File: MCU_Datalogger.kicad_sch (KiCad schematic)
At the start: 25 parts, among them U1 24LC1025, U2 24LC1025, U3 DS1337S_, U4 ATMEGA328P-AU, Y1 Crystal, Y2 Crystal

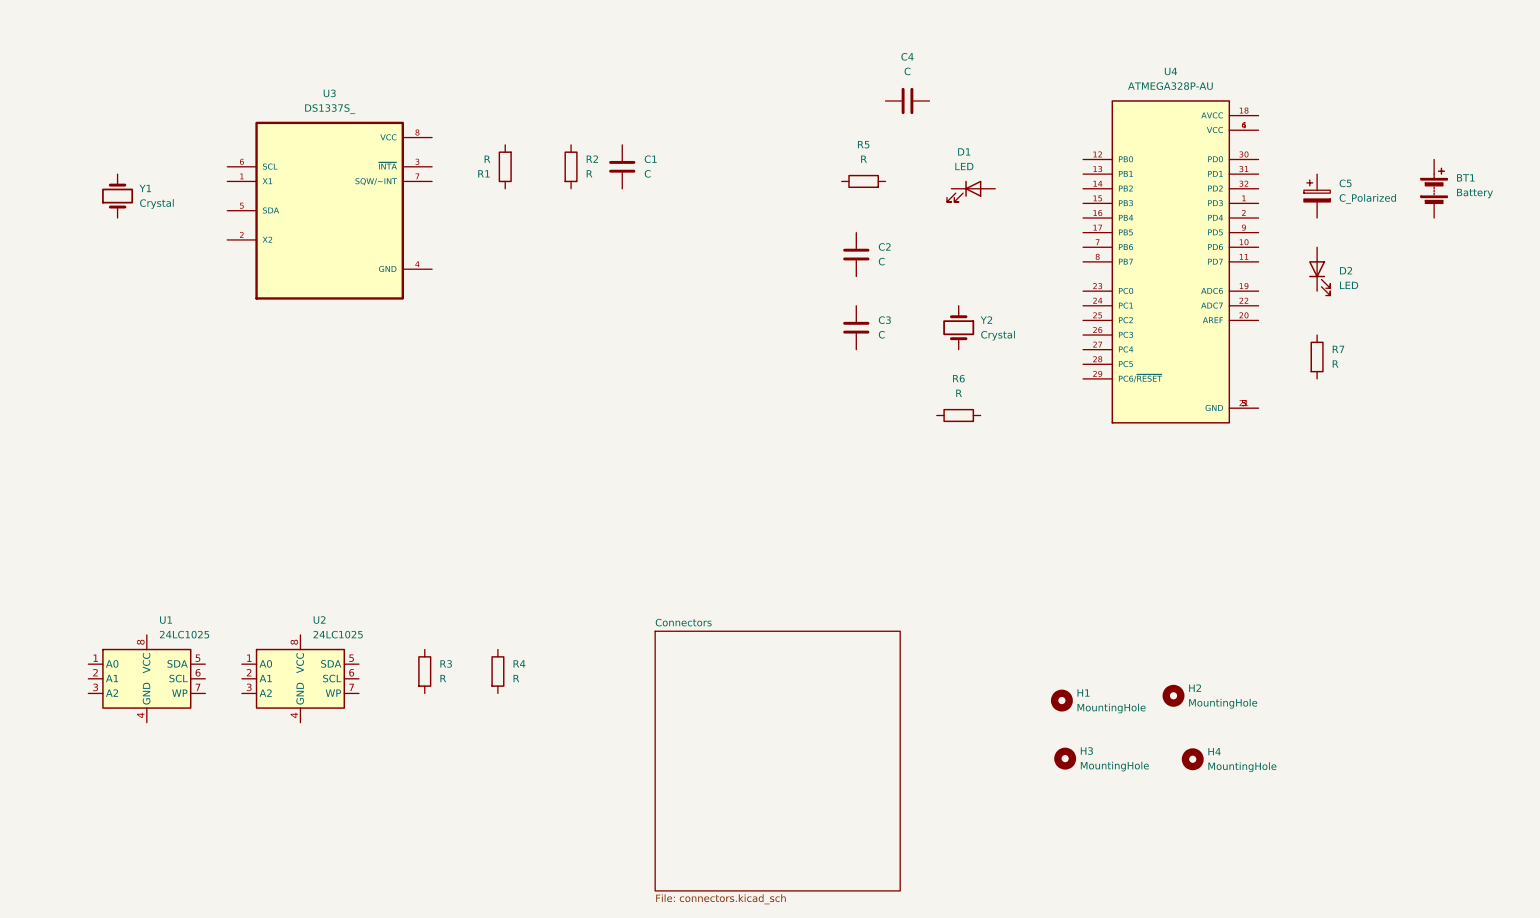
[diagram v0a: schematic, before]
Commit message: Assigned footprints to components
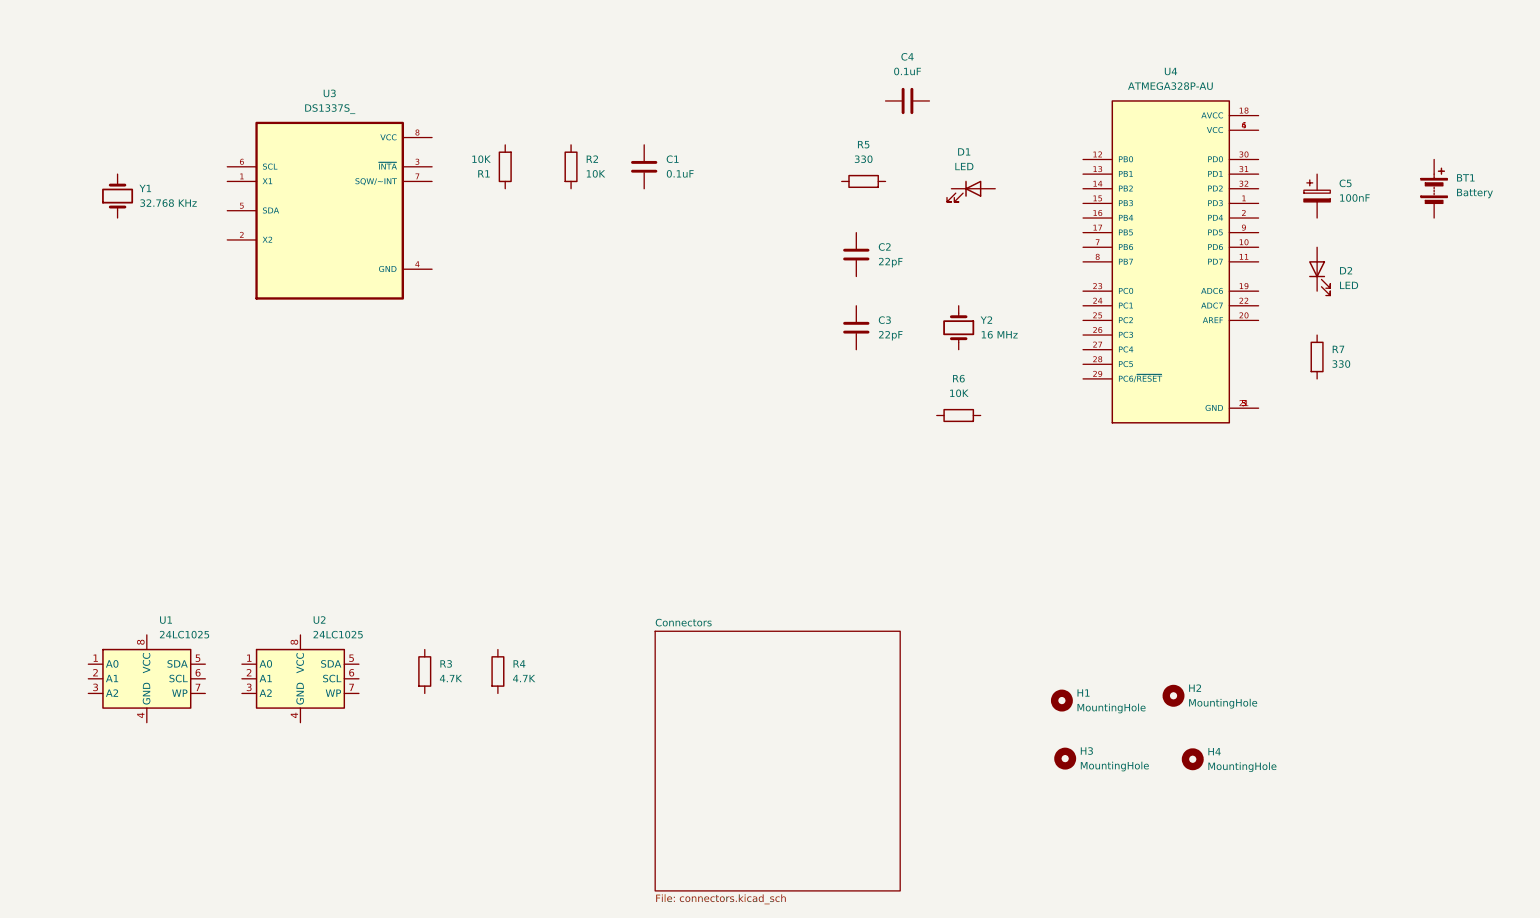
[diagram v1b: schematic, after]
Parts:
- BT1: footprint (none) -> Connector_PinHeader_2.54mm:PinHeader_1x02_P2.54mm_Vertical
- C1, C4: value C -> 0.1uF; footprint (none) -> Capacitor_SMD:C_0805_2012Metric
- C2, C3: value C -> 22pF; footprint (none) -> Capacitor_SMD:C_0805_2012Metric
- C5: value C_Polarized -> 100nF; footprint (none) -> Capacitor_SMD:C_0805_2012Metric
- D1, D2: footprint (none) -> LED_SMD:LED_0805_2012Metric
- H1, H2, H3, H4: footprint (none) -> MountingHole:MountingHole_2.1mm
- R1, R2, R6: value R -> 10K; footprint (none) -> Resistor_SMD:R_0805_2012Metric
- R3, R4: value R -> 4.7K; footprint (none) -> Resistor_SMD:R_0805_2012Metric
- R5, R7: value R -> 330; footprint (none) -> Resistor_SMD:R_0805_2012Metric
- U1, U2: footprint (none) -> Package_SO:SOIC-8_5.3x5.3mm_P1.27mm
- U3: footprint DS1337S_:SOIC127P600X175-8N -> Footprints:SOIC127P600X175-8N
- U4: footprint ATMEGA328P-AU:QFP80P900X900X120-32N -> Footprints:QFP80P900X900X120-32N
- Y1: value Crystal -> 32.768 KHz; footprint (none) -> Crystal:Crystal_SMD_5032-2Pin_5.0x3.2mm_HandSoldering
- Y2: value Crystal -> 16 MHz; footprint (none) -> Crystal:Crystal_SMD_5032-2Pin_5.0x3.2mm_HandSoldering
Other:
- moved on the sheet: C1

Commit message: Added wiring to main sheet
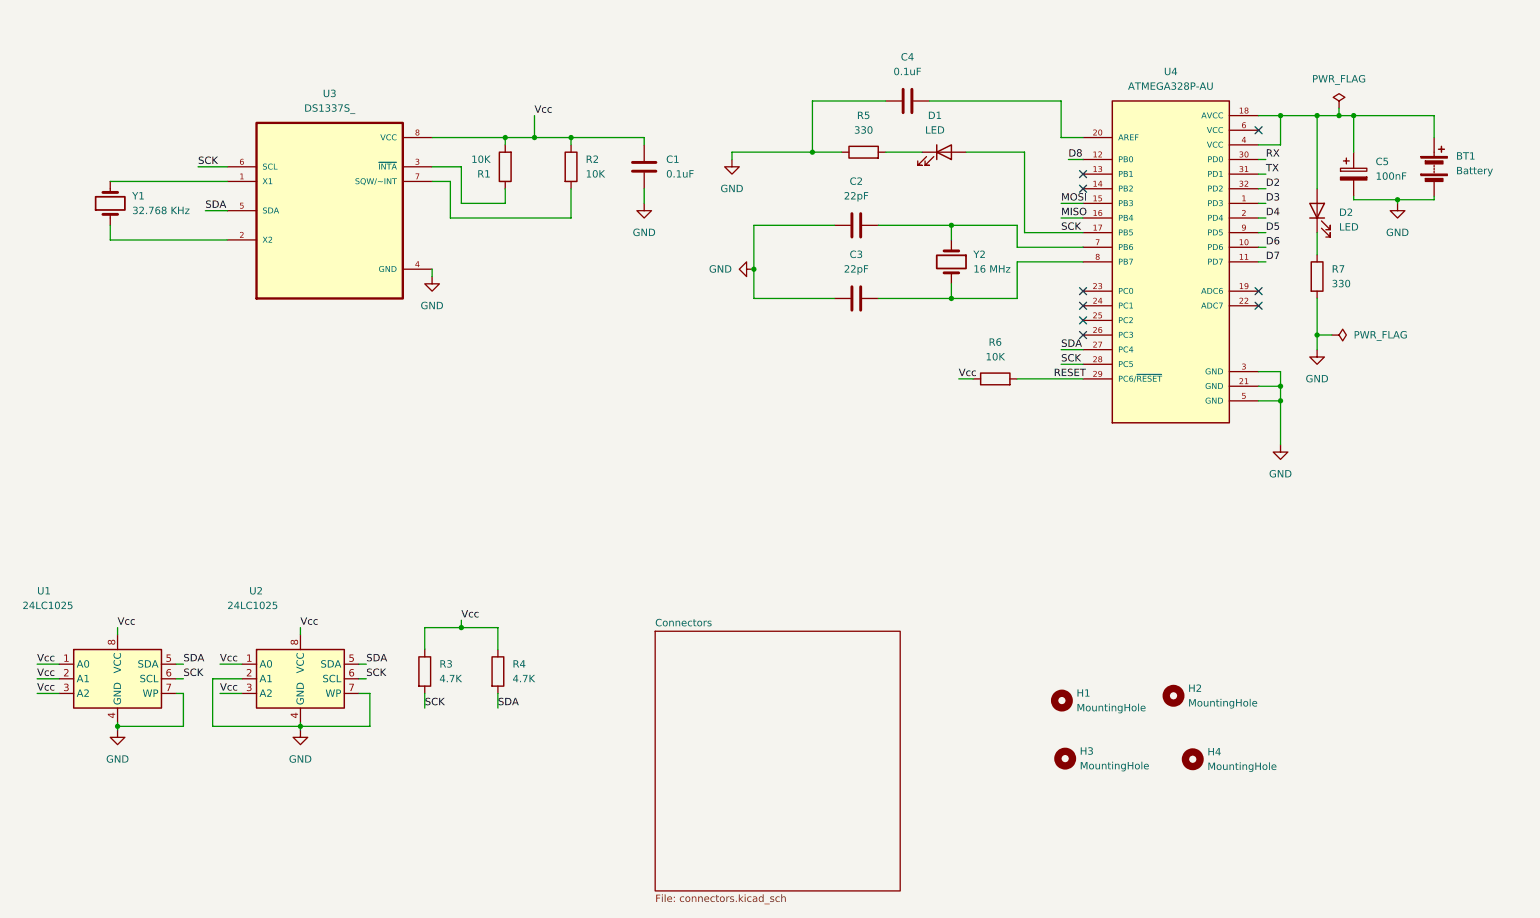
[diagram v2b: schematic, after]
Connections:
- net Vcc: now reaches R6.1
- net Vcc: now also C1.1, R1.2, R2.1, R3.1, R4.1, U1.1 (A0), U1.2 (A1), U1.3 (A2), U1.8 (VCC), U2.1 (A0), U2.3 (A2), U2.8 (VCC), U3.8 (VCC)
- net RESET: now reaches R6.2
- net RESET: now also U4.29 (PC6/~{RESET})
- net at BT1.1 (+): now also C5.1, D2.2 (A), U4.18 (AVCC), U4.4 (VCC)
- net GND: now reaches BT1.2 (-)
- net GND: now also C1.2, C2.1, C3.1, C4.1, C5.2, R5.1, R7.2, U1.4 (GND), U1.7 (WP), U2.2 (A1), U2.4 (GND), U2.7 (WP), U3.4 (GND), U4.21 (GND), U4.3 (GND), U4.5 (GND)
- net D3: now reaches U4.1 (PD3)
- net D6: now reaches U4.10 (PD6)
- net D7: now reaches U4.11 (PD7)
- net D8: now reaches U4.12 (PB0)
- net MOSI: now reaches U4.15 (PB3)
- net MISO: now reaches U4.16 (PB4)
- net SCK: now reaches U4.17 (PB5)
- net SCK: now also D1.2 (A), R3.2, U1.6 (SCL), U2.6 (SCL), U3.6 (SCL), U4.28 (PC5)
- net D4: now reaches U4.2 (PD4)
- net at U4.20 (AREF): now also C4.2
- net SDA: now reaches U4.27 (PC4)
- net SDA: now also R4.2, U1.5 (SDA), U2.5 (SDA), U3.5 (SDA)
- net RX: now reaches U4.30 (PD0)
- net TX: now reaches U4.31 (PD1)
- net D2: now reaches U4.32 (PD2)
- net at U4.6 (VCC): no longer U4.4 (VCC)
- net at U4.7 (PB6): now also C2.2, Y2.1
- net at U4.8 (PB7): now also C3.2, Y2.2
- net D5: now reaches U4.9 (PD5)
- net at R1.1: now also U3.3 (~{INTA})
- net at R5.2: now also D1.1 (K)
- net at R2.2: now also U3.7 (SQW/~INT)
- net at D2.1 (K): now also R7.1
- net at Y1.1: now also U3.2 (X2)
- net at Y1.2: now also U3.1 (X1)
- no-connect marks 0 -> 9
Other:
- moved on the sheet: BT1, C2, C3, C5, D1, D2, R5, R6, R7, U1, Y1, Y2

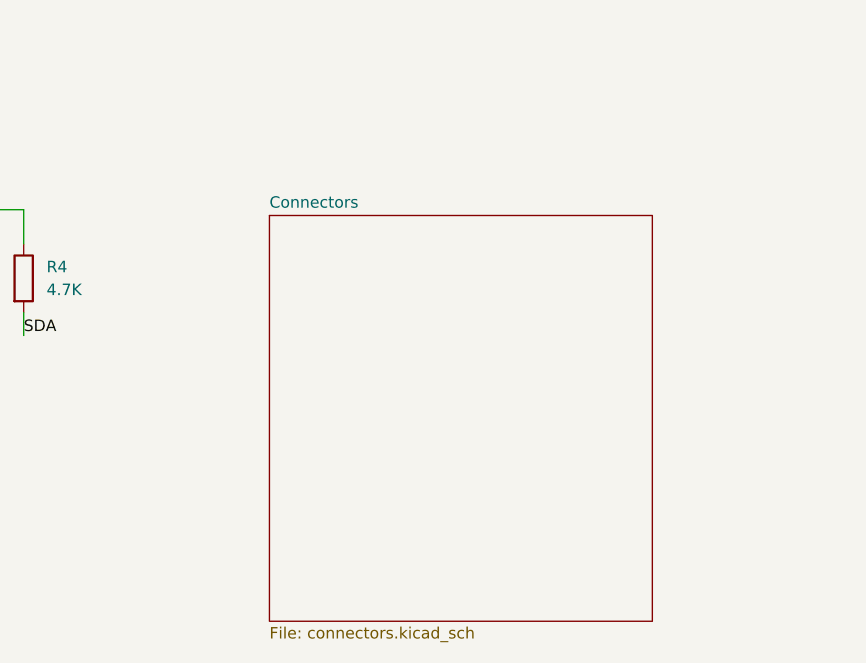
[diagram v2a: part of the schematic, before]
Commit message: Completed wiring of second sheet + added connectection between the 2 sheets
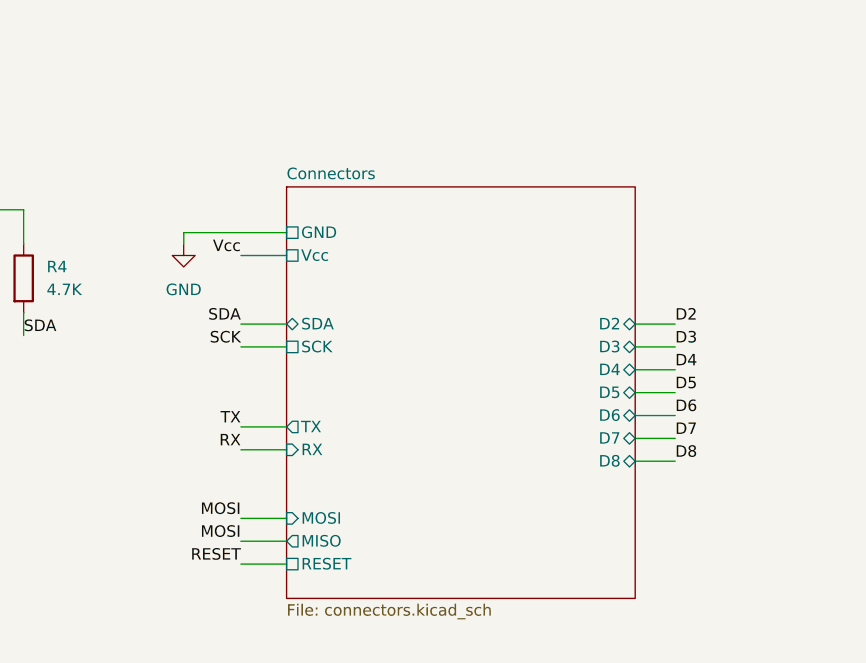
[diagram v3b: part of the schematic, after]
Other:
- sheet Connectors ports: added D2, D3, D4, D5, D6, D7, D8, GND, MISO, MOSI, RESET, RX, SCK, SDA, TX, Vcc; removed none

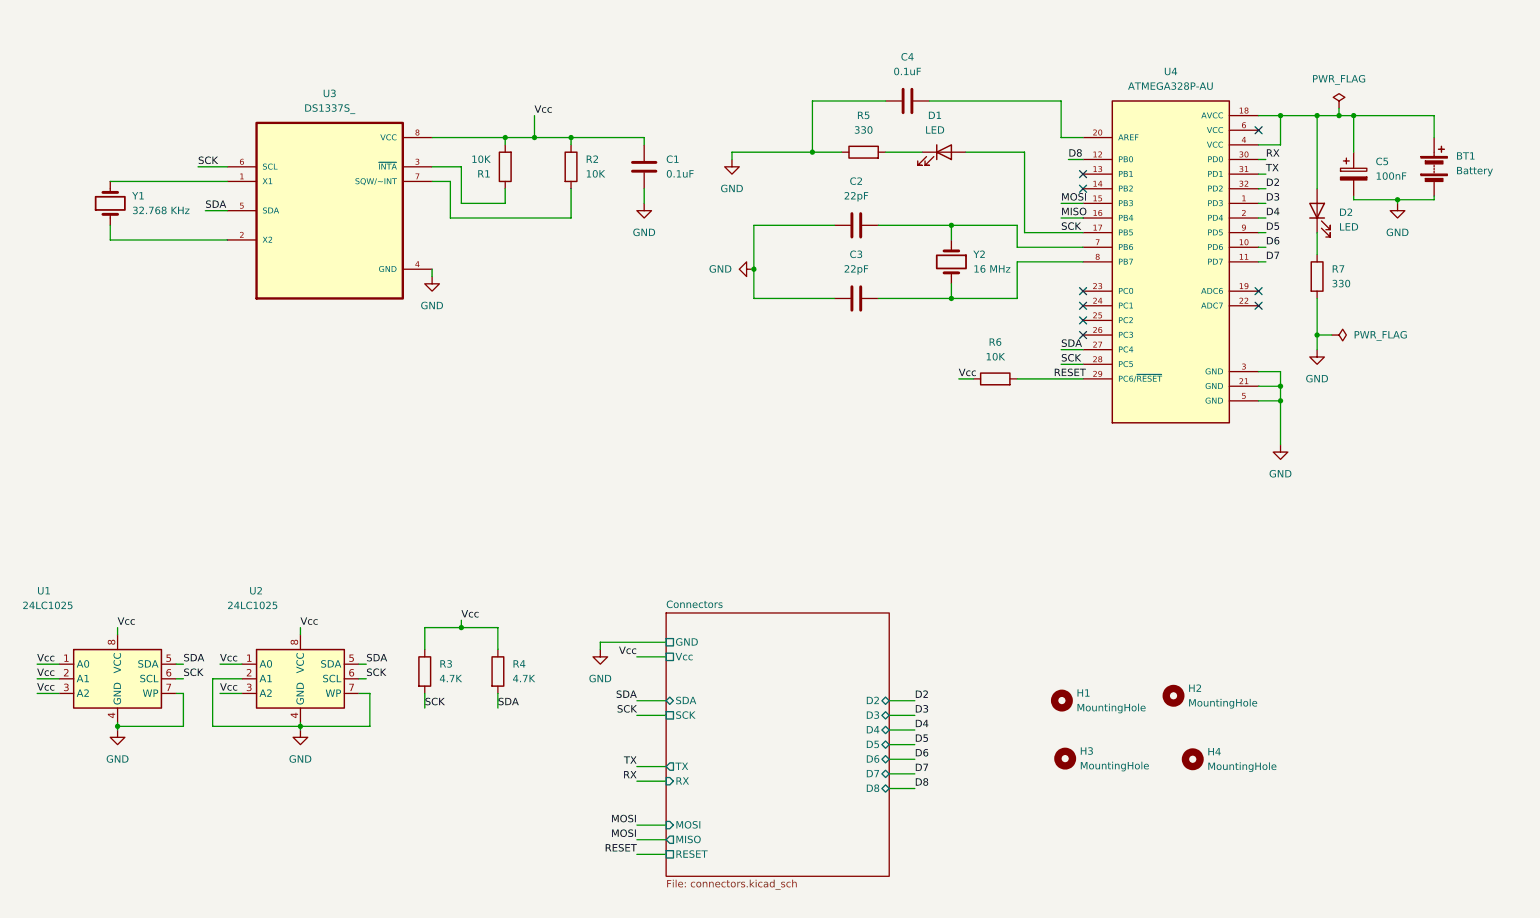
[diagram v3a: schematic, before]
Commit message: Added comments and made the schematics neat
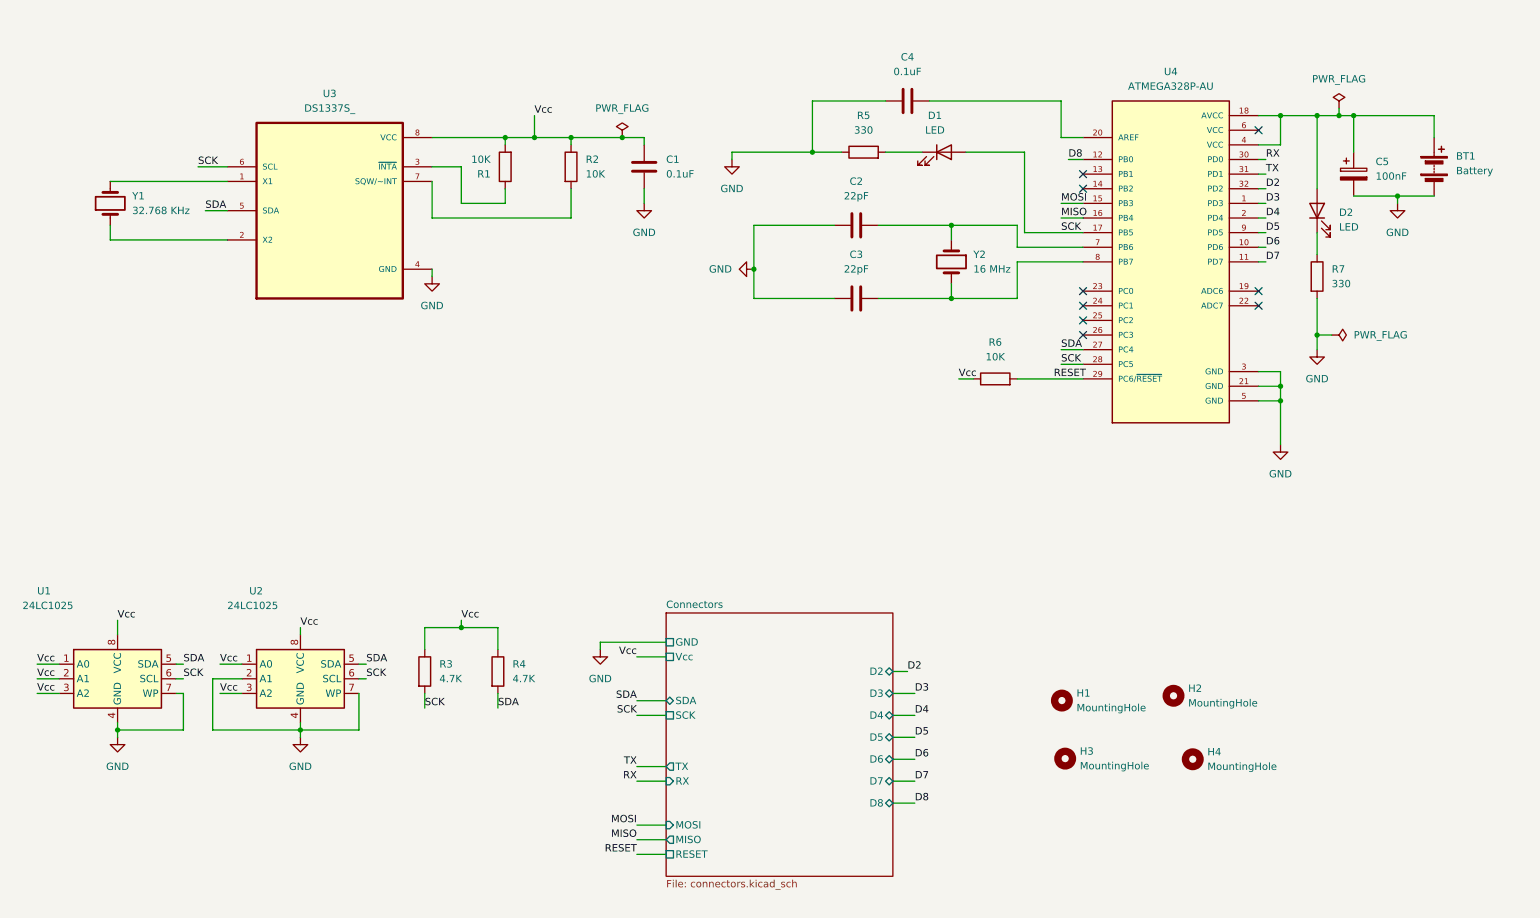
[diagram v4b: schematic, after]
